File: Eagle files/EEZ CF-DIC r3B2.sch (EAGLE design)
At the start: 236 parts, among them IC1 MC79L05, IC2 LP2951, IC3 VIPer35L, IC4 SI8233BB-D-IS1, IC5 LM5041B, IC6 IR11688STRPBF, IC7 TL072, IC8 TL103W, IC9 TL431, P1 T910W-50K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

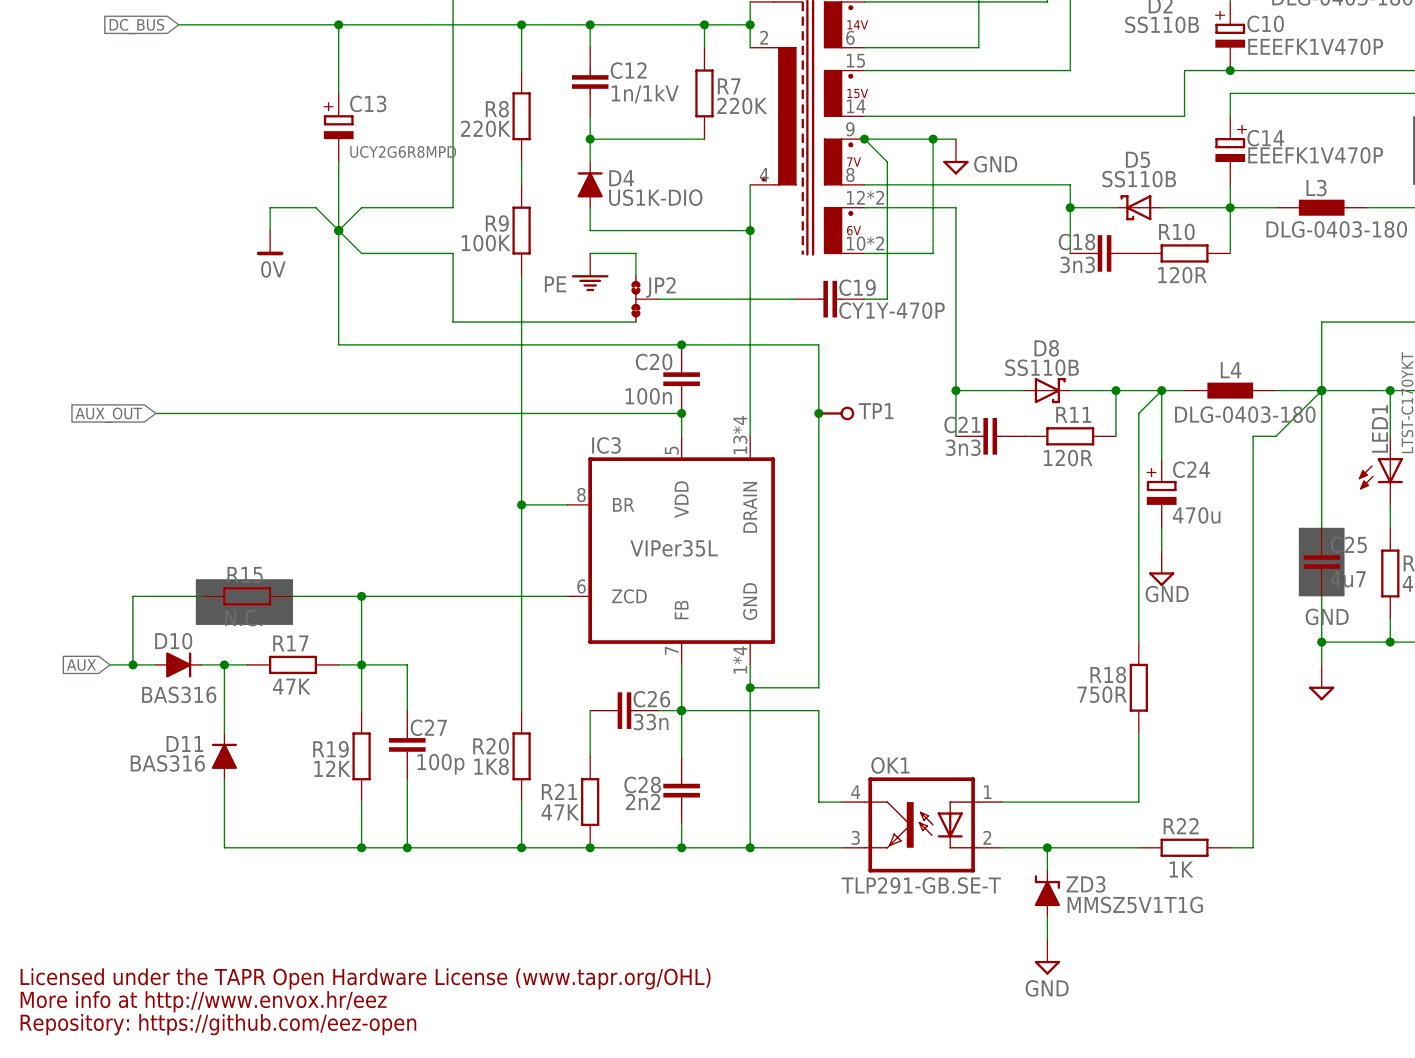
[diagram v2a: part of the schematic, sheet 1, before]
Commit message: fixed .sch - .brd inconsistency reported by Eagle 7.x
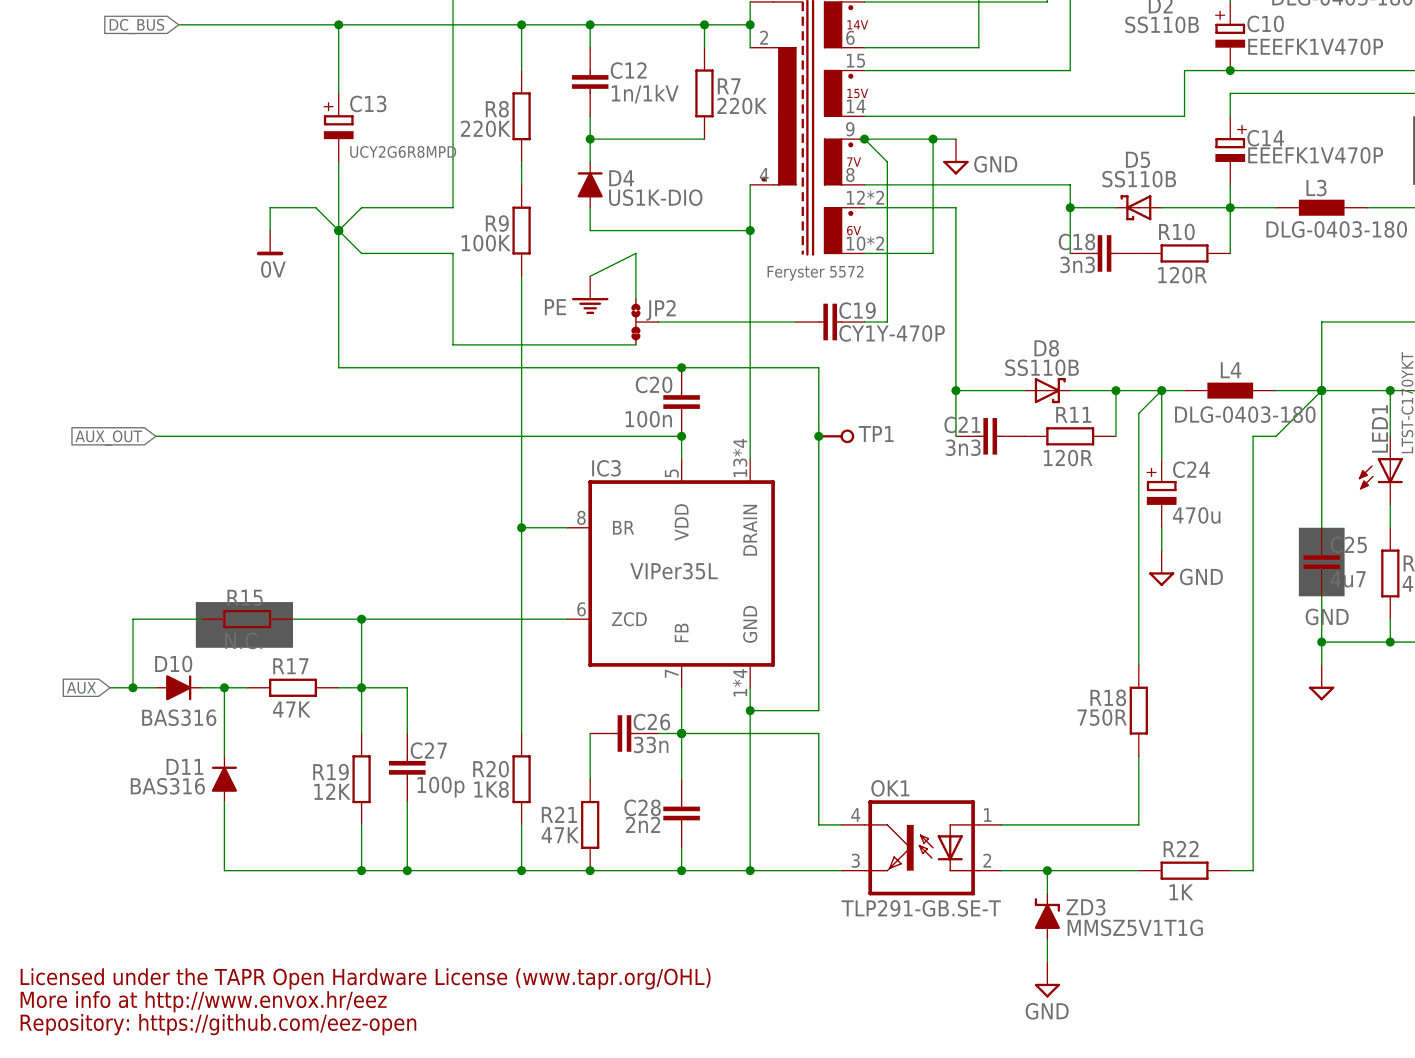
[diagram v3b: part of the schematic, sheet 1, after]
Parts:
- TR1: value (none) -> Feryster 5572
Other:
- moved on the sheet: C19, C20, C26, C27, C28, D10, D11, IC3, JP2, OK1, R15, R17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

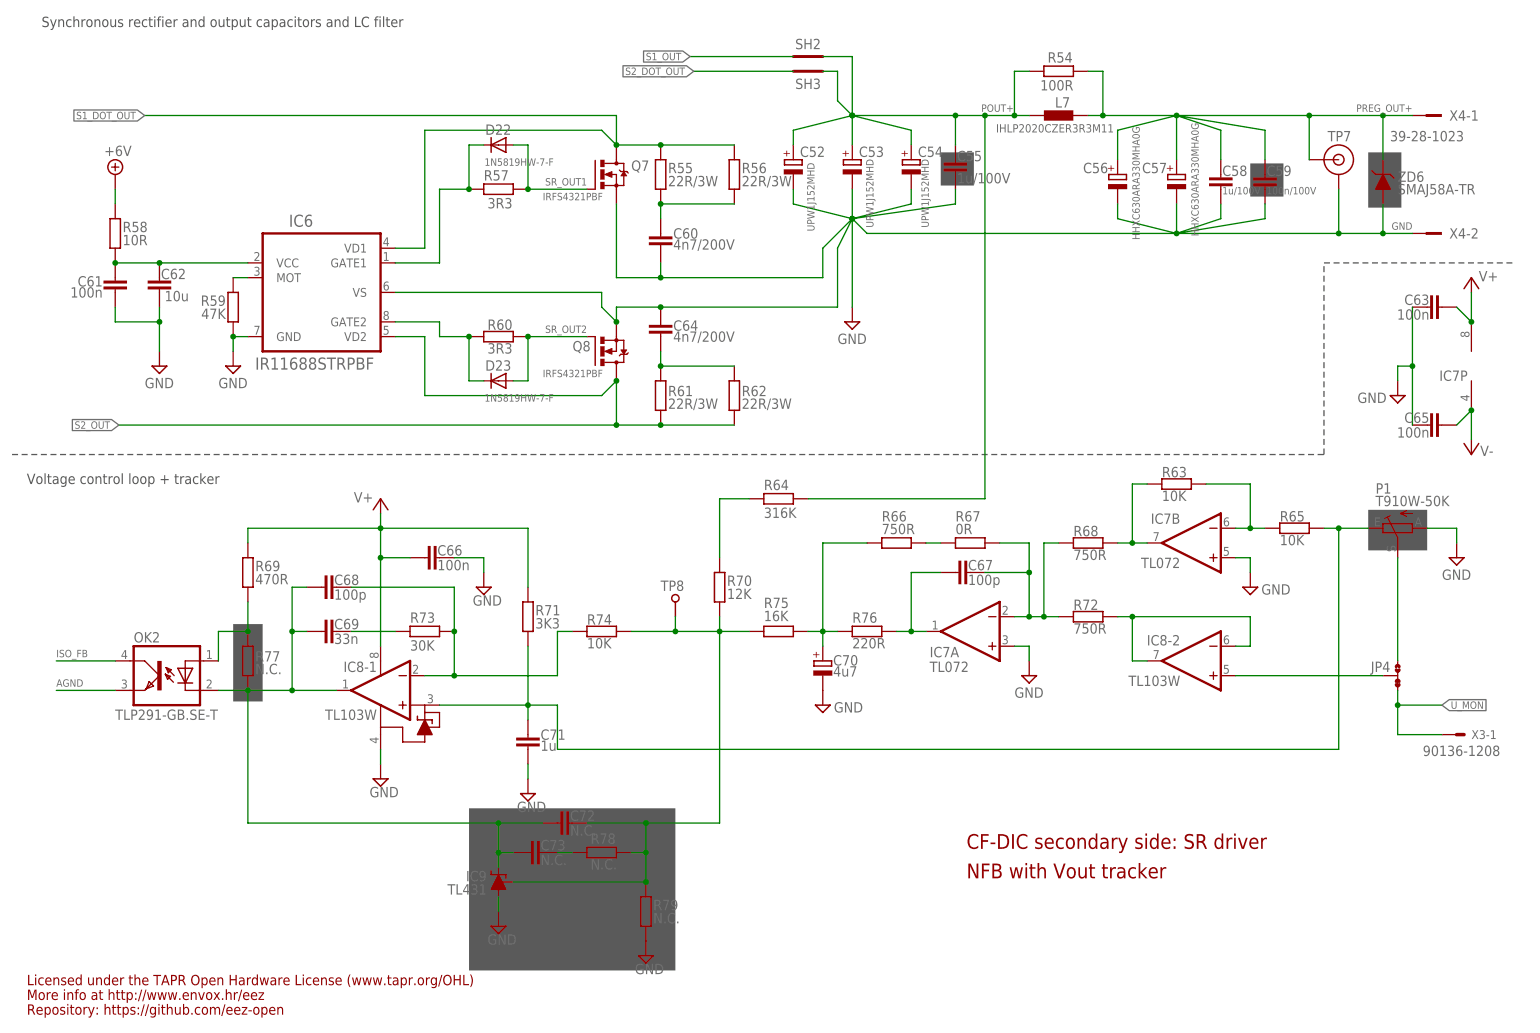
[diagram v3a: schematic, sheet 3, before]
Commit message: BOM update, optional RC added at the output terminals
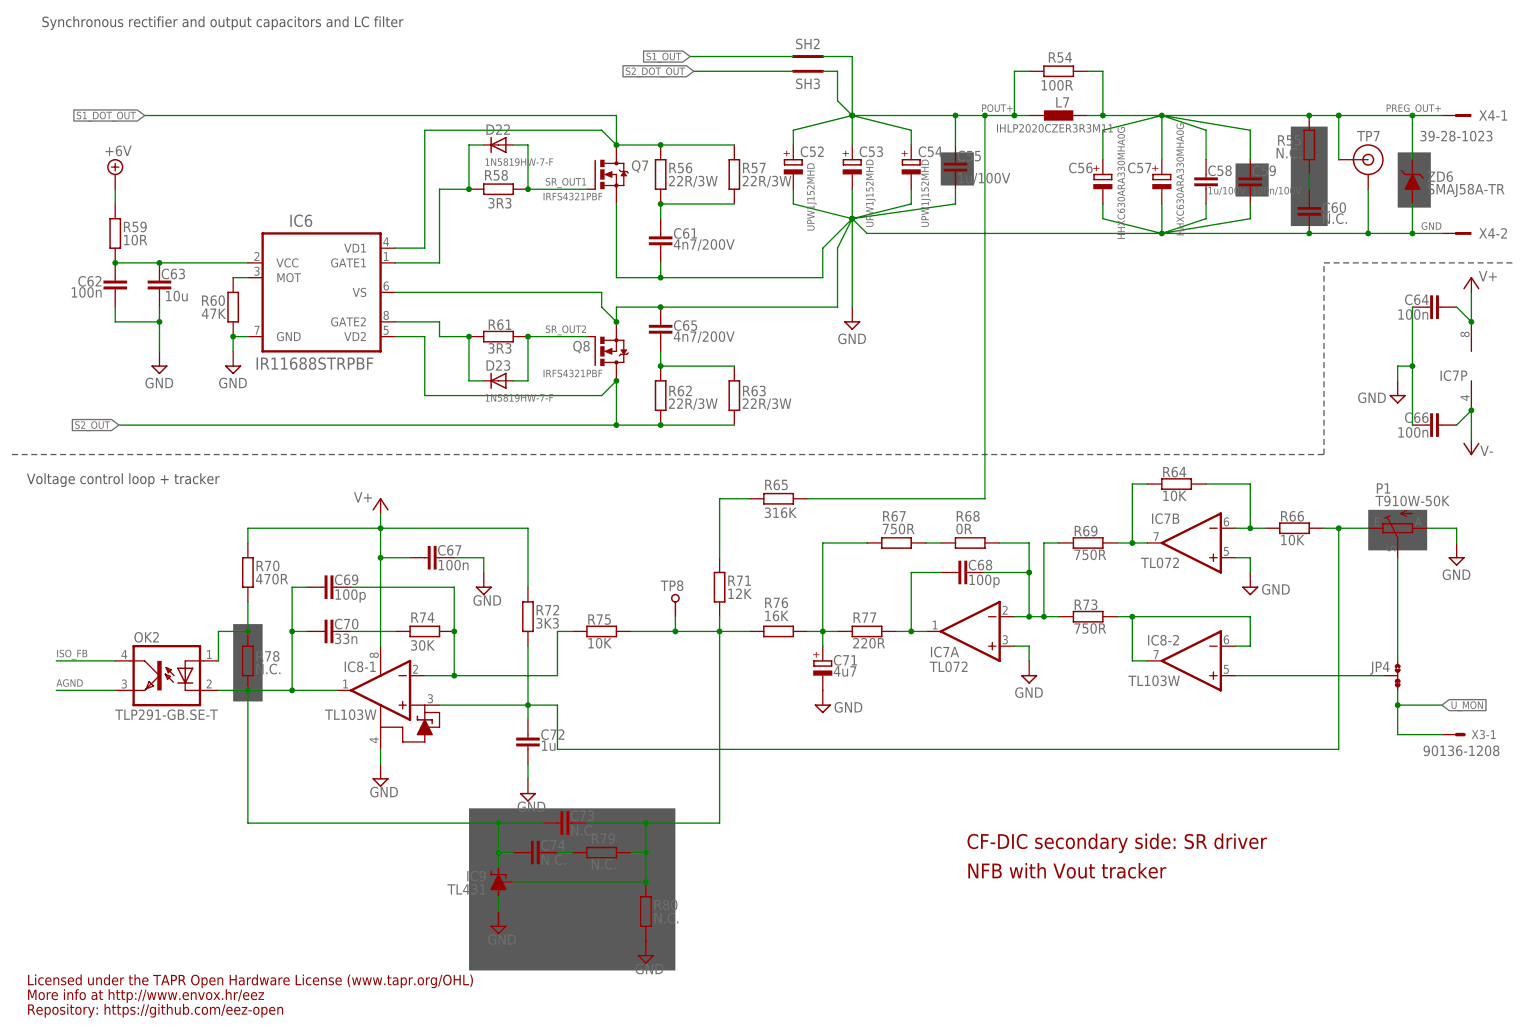
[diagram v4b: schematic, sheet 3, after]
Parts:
- added C74: N.C., rcl:C-EUC0805
- added R80: N.C., rcl:R-EU_R0805
- C42: device rcl:C-EUC0805 -> rcl:C-EUC0603
- C60: value 4n7/200V -> N.C.
- C61, C65: value 100n -> 4n7/200V; device rcl:C-EUC0603 -> rcl:C-EUC1206
- C62: value 10u -> 100n; device rcl:C-EUC1210 -> rcl:C-EUC0603
- C63: value 100n -> 10u; device rcl:C-EUC0603 -> rcl:C-EUC1210
- C64: value 4n7/200V -> 100n; device rcl:C-EUC1206 -> rcl:C-EUC0603
- C67: value 100p -> 100n; device rcl:C-EUC0805 -> rcl:C-EUC0603
- C69: value 33n -> 100p
- C70: value 4u7 -> 33n; device EEZ_Lib1:ECAP1206 -> rcl:C-EUC0805
- C71: value 1u -> 4u7; device rcl:C-EUC0805 -> EEZ_Lib1:ECAP1206
- C72: value N.C. -> 1u
- R55: value 22R/3W -> N.C.; device rcl:R-EU_R2512 -> rcl:R-EU_R1210
- R57: value 3R3 -> 22R/3W; device rcl:R-EU_R0805 -> rcl:R-EU_R2512
- R58: value 10R -> 3R3
- R59: value 47K -> 10R
- R60: value 3R3 -> 47K
- R61: value 22R/3W -> 3R3; device rcl:R-EU_R2512 -> rcl:R-EU_R0805
- R63: value 10K -> 22R/3W; device rcl:R-EU_R0805 -> rcl:R-EU_R2512
- R64: value 316K -> 10K
- R65: value 10K -> 316K
- R66: value 750R -> 10K
- R67: value 0R -> 750R
- R68: value 750R -> 0R
- R69: value 470R -> 750R
- R70: value 12K -> 470R
- R71: value 3K3 -> 12K
- R72: value 750R -> 3K3
- R73: value 30K -> 750R
- R74: value 10K -> 30K
- R75: value 16K -> 10K
- R76: value 220R -> 16K
- R77: value N.C. -> 220R
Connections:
- new net N$8: C60.2, R55.1
- net +6V: now also R59.1; no longer R58.1
- net FB: now also C73.2, R71.1, R76.2, R80.2; no longer C72.2, R70.1, R74.2, R78.2
- net GND: now also C60.1, C67.2, C71.-, C72.2, R60.2, R80.1; no longer C60.2, C70.-, C71.2, R59.2, R79.1
- net N$1: now also C68.2, R68.2, R69.1, R73.1; no longer C67.2, R67.2, R68.1, R72.1
- net N$10: now also C69.2, R75.1; no longer C68.2, R73.1
- net N$12: now also R65.1, R71.2; no longer R64.1, R70.2
- net N$132: now also R64.2, R66.1; no longer R63.2, R65.1
- net N$134: now also C68.1, R77.2; no longer C67.1, R76.2
- net N$17: now also C74.2, R79.1; no longer C73.2, R78.1
- net N$18: now also R60.1; no longer R59.1
- net N$53: now also R64.1, R69.2; no longer R63.1, R68.2
- net N$6: now also C63.1, R59.2; no longer C61.1, R58.2
- net N$64: now also R67.2, R68.1; no longer R66.2, R67.1
- net N$66: now also C61.1, R57.2; no longer C60.1, R55.2
- net N$67: now also C65.1, R63.2; no longer C64.1, R61.2
- net N$7: now also C72.1, R66.2, R72.1; no longer C71.1, R65.2, R71.1
- net N$74: now also R58.2; no longer R57.2
- net N$75: now also R61.2; no longer R60.2
- net N$76: now also C70.1, C74.1, R78.2; no longer C68.1, C72.1, R77.2
- net N$9: now also C70.2, R74.2; no longer C69.2, R73.2
- net NFB_OFFSET: now also C71.+, R67.1, R77.1; no longer C70.+, R66.1, R75.1
- net OK_A: now also R70.1, R78.1; no longer R69.1, R77.1
- net POUT+: now also R65.2; no longer R64.2
- net PREG_OUT+: now also R55.2
- net S1_DOT_OUT: now also R57.1; no longer R55.1
- net S2_OUT: now also R63.1; no longer R61.1
- net SR_OUT1: now also R58.1; no longer R57.1
- net SR_OUT2: now also R61.1; no longer R60.1
- net U_MON1: now also R73.2; no longer R72.2
- net V+: now also C64.1, C67.1, R70.2, R72.2; no longer C63.1, C66.1, R69.2, R71.2
- net V-: now also C66.1; no longer C65.1
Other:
- moved on the sheet: C56, C57, C58, C59, C60, C61, C62, C63, C64, C65, C66, C67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
